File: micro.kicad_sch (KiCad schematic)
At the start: 19 parts, among them U101 STM32G474RETx

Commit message: Added SPI
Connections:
- net DIR1: now also U101.43 (PA9); no longer U101.21 (PA7)
- net DIR2: now also U101.45 (PA11); no longer U101.43 (PA9)
- net SPI_SCK: now reaches U101.19 (PA5)
- net SPI_MISO: now reaches U101.20 (PA6)
- new net SPI_MOSI: U101.21 (PA7)
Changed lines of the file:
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@@
+	(wire
+		(pts
+			(xy 156.21 54.61) (xy 170.18 54.61)
+		)
+		(stroke
+			(width 0)
+			(type default)
+		)
+	)
 	(wire
 		(pts
@@
 	(wire
 		(pts
+			(xy 156.21 64.77) (xy 201.93 64.77)
+		)
+		(stroke
+			(width 0)
+			(type default)
+		)
+	)
+	(wire
+		(pts
 			(xy 82.55 46.99) (xy 120.65 46.99)
 		)
@@
 	(wire
 		(pts
-			(xy 156.21 59.69) (xy 201.93 59.69)
-		)
-		(stroke
-			(width 0)
-			(type default)
-		)
-	)
-	(wire
-		(pts
 			(xy 156.21 80.01) (xy 170.18 80.01)
 		)
@@
 	(wire
 		(pts
+			(xy 156.21 59.69) (xy 170.18 59.69)
+		)
+		(stroke
+			(width 0)
+			(type default)
+		)
+	)
+	(wire
+		(pts
 			(xy 143.51 30.48) (xy 140.97 30.48)
 		)
@@
 	(wire
 		(pts
-			(xy 156.21 64.77) (xy 201.93 64.77)
-		)
-		(stroke
-			(width 0)
-			(type default)
-		)
-	)
-	(wire
-		(pts
 			(xy 184.15 49.53) (xy 190.5 49.53)
 		)
@@
 	(wire
 		(pts
+			(xy 156.21 69.85) (xy 201.93 69.85)
+		)
+		(stroke
+			(width 0)
+			(type default)
+		)
+	)
+	(wire
+		(pts
 			(xy 240.03 151.13) (xy 240.03 147.32)
 		)
@@
 		(pts
 			(xy 240.03 147.32) (xy 240.03 143.51)
+		)
+		(stroke
+			(width 0)
+			(type default)
+		)
+	)
+	(wire
+		(pts
+			(xy 156.21 57.15) (xy 170.18 57.15)
 		)
 		(stroke
@@
 		)
 	)
+	(hierarchical_label "SPI_MOSI"
+		(shape input)
+		(at 170.18 59.69 0)
+		(effects
+			(font
+				(size 1.27 1.27)
+			)
+			(justify left)
+		)
+	)
 	(hierarchical_label "T_SWO"
 		(shape bidirectional)
@@
 	(hierarchical_label "DIR2"
 		(shape output)
-		(at 201.93 64.77 0)
+		(at 201.93 69.85 0)
 		(effects
 			(font
@@
 		)
 	)
+	(hierarchical_label "SPI_SCK"
+		(shape input)
+		(at 170.18 54.61 0)
+		(effects
+			(font
+				(size 1.27 1.27)
+			)
+			(justify left)
+		)
+	)
 	(hierarchical_label "DIR1"
 		(shape output)
-		(at 201.93 59.69 0)
+		(at 201.93 64.77 0)
 		(effects
 			(font
@@
 		)
 	)
+	(hierarchical_label "SPI_MISO"
+		(shape output)
+		(at 170.18 57.15 0)
+		(effects
+			(font
+				(size 1.27 1.27)
+			)
+			(justify left)
+		)
+	)

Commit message: starting layout
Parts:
- R501: renamed from R214; footprint Resistor_SMD:R_0805_2012Metric_Pad1.20x1.40mm_HandSolder -> Resistor_SMD:R_0603_1608Metric_Pad0.98x0.95mm_HandSolder
- R502: renamed from R206; footprint Resistor_SMD:R_0805_2012Metric_Pad1.20x1.40mm_HandSolder -> Resistor_SMD:R_0603_1608Metric_Pad0.98x0.95mm_HandSolder
- R503: renamed from R207; footprint Resistor_SMD:R_0805_2012Metric_Pad1.20x1.40mm_HandSolder -> Resistor_SMD:R_0603_1608Metric_Pad0.98x0.95mm_HandSolder
- R504: renamed from R226; footprint Resistor_SMD:R_0805_2012Metric_Pad1.20x1.40mm_HandSolder -> Resistor_SMD:R_0603_1608Metric_Pad0.98x0.95mm_HandSolder
- R505: renamed from R210; footprint Resistor_SMD:R_0805_2012Metric_Pad1.20x1.40mm_HandSolder -> Resistor_SMD:R_0603_1608Metric_Pad0.98x0.95mm_HandSolder
- R506: renamed from R211; footprint Resistor_SMD:R_0805_2012Metric_Pad1.20x1.40mm_HandSolder -> Resistor_SMD:R_0603_1608Metric_Pad0.98x0.95mm_HandSolder
- R507: renamed from R208; footprint Resistor_SMD:R_0805_2012Metric_Pad1.20x1.40mm_HandSolder -> Resistor_SMD:R_0603_1608Metric_Pad0.98x0.95mm_HandSolder
- R508: renamed from R209; footprint Resistor_SMD:R_0805_2012Metric_Pad1.20x1.40mm_HandSolder -> Resistor_SMD:R_0603_1608Metric_Pad0.98x0.95mm_HandSolder
- renumbered C207 to C501, C208 to C502, C218 to C503, C206 to C504, C205 to C505, C204 to C506, C203 to C507, R227 to R509, R228 to R510, R232 to R511, U101 to U501
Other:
- moved on the sheet: R509, R510

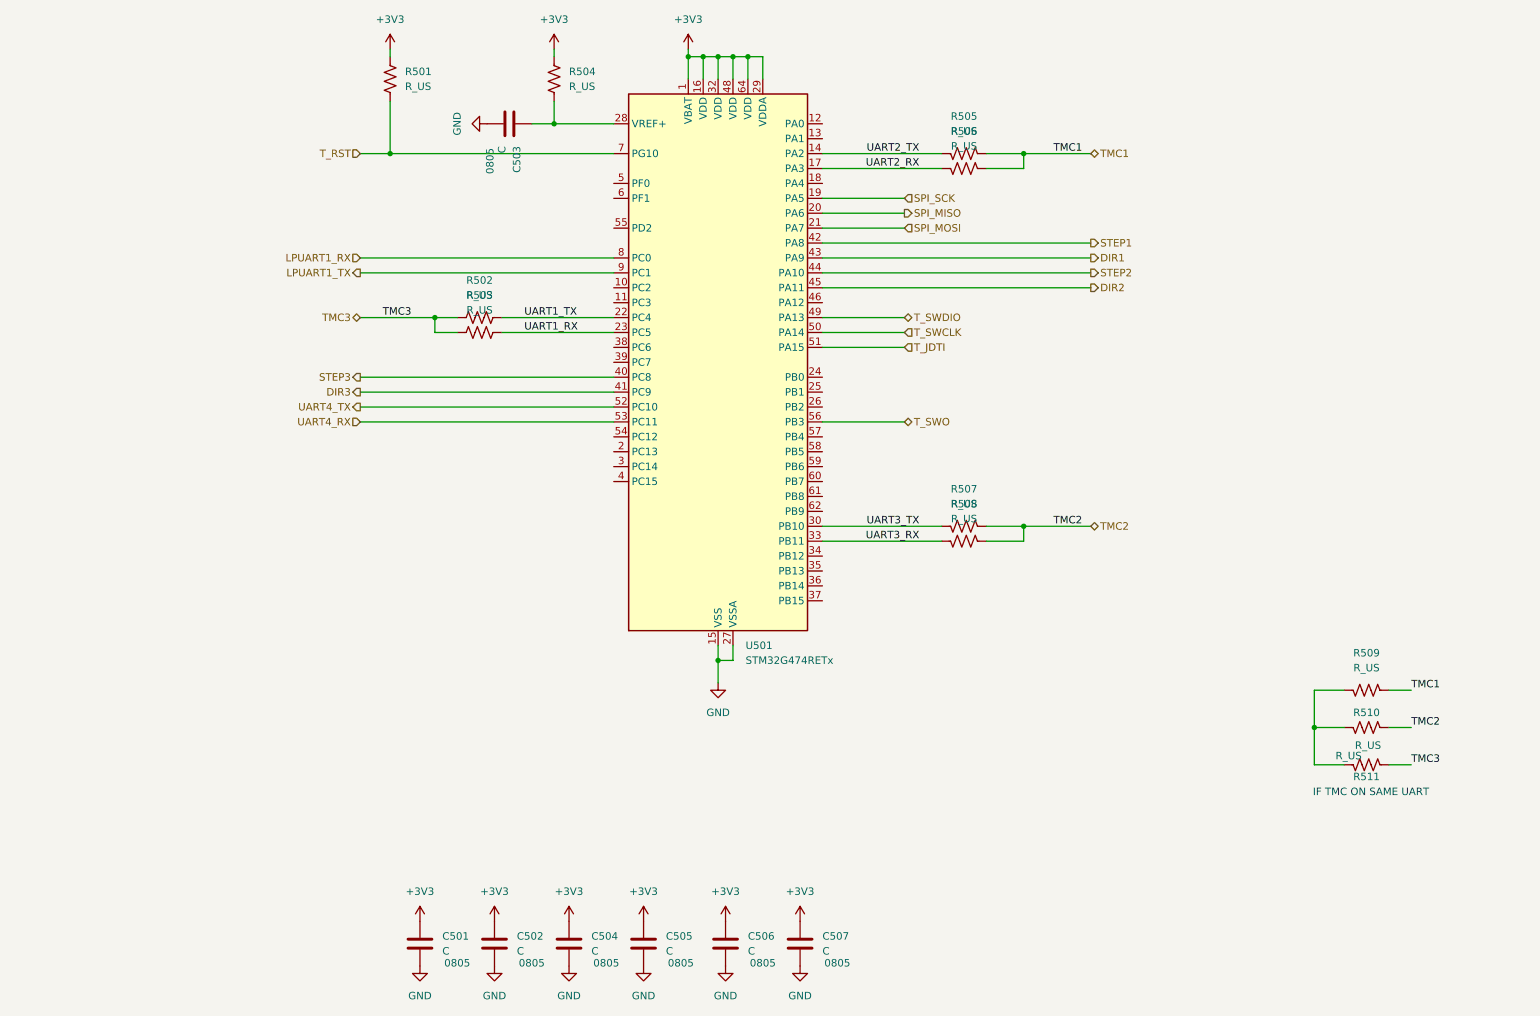
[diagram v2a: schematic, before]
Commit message: Add net class
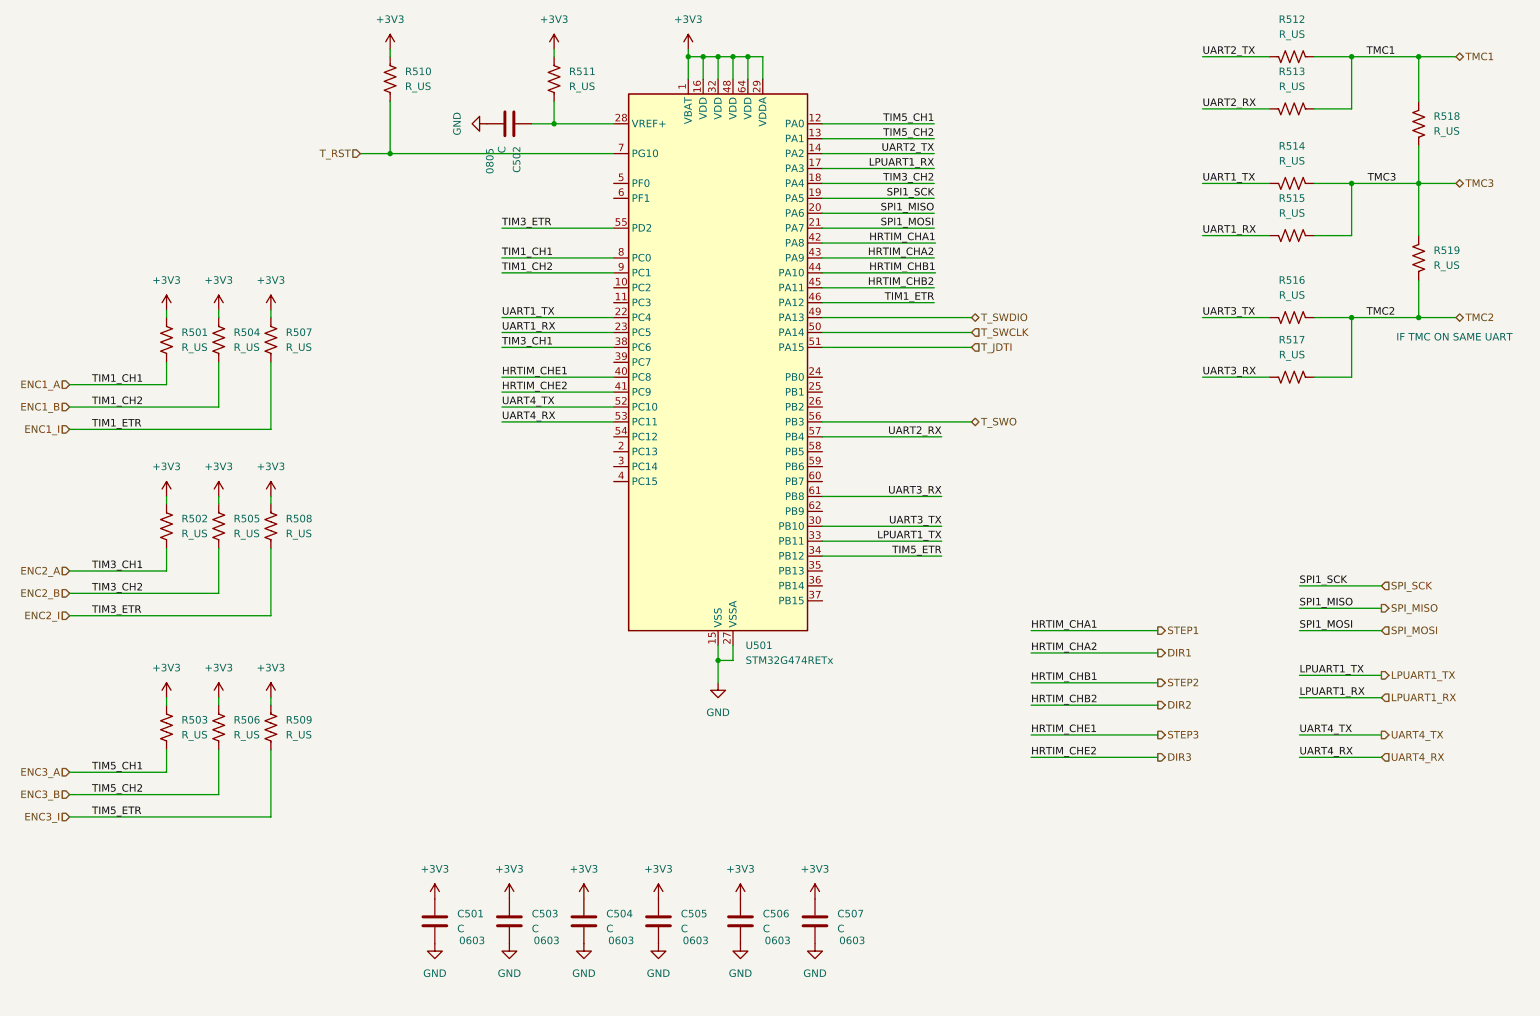
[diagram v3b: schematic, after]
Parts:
- removed C502: C, Capacitor_SMD:C_0805_2012Metric_Pad1.18x1.45mm_HandSolder, symbol Device:C
- removed R510, R511: R_US, Resistor_SMD:R_0805_2012Metric_Pad1.20x1.40mm_HandSolder, symbol Device:R_US
- added C503: C, Capacitor_SMD:C_0603_1608Metric_Pad1.08x0.95mm_HandSolder, symbol Device:C
- added R501, R502, R503, R504, R505, R506, R507, R508: R_US, Resistor_SMD:R_0603_1608Metric_Pad0.98x0.95mm_HandSolder, symbol Device:R_US
- added R518, R519: R_US, Resistor_SMD:R_0805_2012Metric_Pad1.20x1.40mm_HandSolder, symbol Device:R_US
- C501, C504, C505, C506, C507: footprint Capacitor_SMD:C_0805_2012Metric_Pad1.18x1.45mm_HandSolder -> Capacitor_SMD:C_0603_1608Metric_Pad1.08x0.95mm_HandSolder; Size 0805 -> 0603
- R509: footprint Resistor_SMD:R_0805_2012Metric_Pad1.20x1.40mm_HandSolder -> Resistor_SMD:R_0603_1608Metric_Pad0.98x0.95mm_HandSolder
- renumbered C503 to C502, R501 to R510, R504 to R511, R505 to R512, R506 to R513, R502 to R514, R503 to R515, R507 to R516, R508 to R517
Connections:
- net +3V3: now also R509.2, C503.1, R501.2, R502.2, R503.2, R504.2, R505.2, R506.2, R507.2, R508.2
- net GND: now also C503.2
- net LPUART1_RX: now also U501.17 (PA3); no longer U501.8 (PC0)
- net LPUART1_TX: now also U501.33 (PB11); no longer U501.9 (PC1)
- net TMC1: now also R518.1; no longer R509.1
- net TMC2: now also R519.2
- net TMC3: now also R518.2, R519.1
- net UART2_RX: now also U501.57 (PB4); no longer U501.17 (PA3)
- net UART3_RX: now also U501.61 (PB8); no longer U501.33 (PB11)
- net ENC3_A: now reaches U501.12 (PA0)
- net ENC3_A: now also R503.1
- net ENC3_B: now reaches U501.13 (PA1)
- net ENC3_B: now also R506.1
- net ENC2_B: now reaches U501.18 (PA4)
- net ENC2_B: now also R505.1
- net ENC3_I: now reaches U501.34 (PB12)
- net ENC3_I: now also R509.1
- net ENC2_A: now reaches U501.38 (PC6)
- net ENC2_A: now also R502.1
- net ENC1_I: now reaches U501.46 (PA12)
- net ENC1_I: now also R507.1
- net ENC2_I: now reaches U501.55 (PD2)
- net ENC2_I: now also R508.1
- new net ENC1_A: R501.1, U501.8 (PC0)
- new net ENC1_B: R504.1, U501.9 (PC1)
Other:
- moved on the sheet: C501, R512, R513, R514, R515, R516, R517

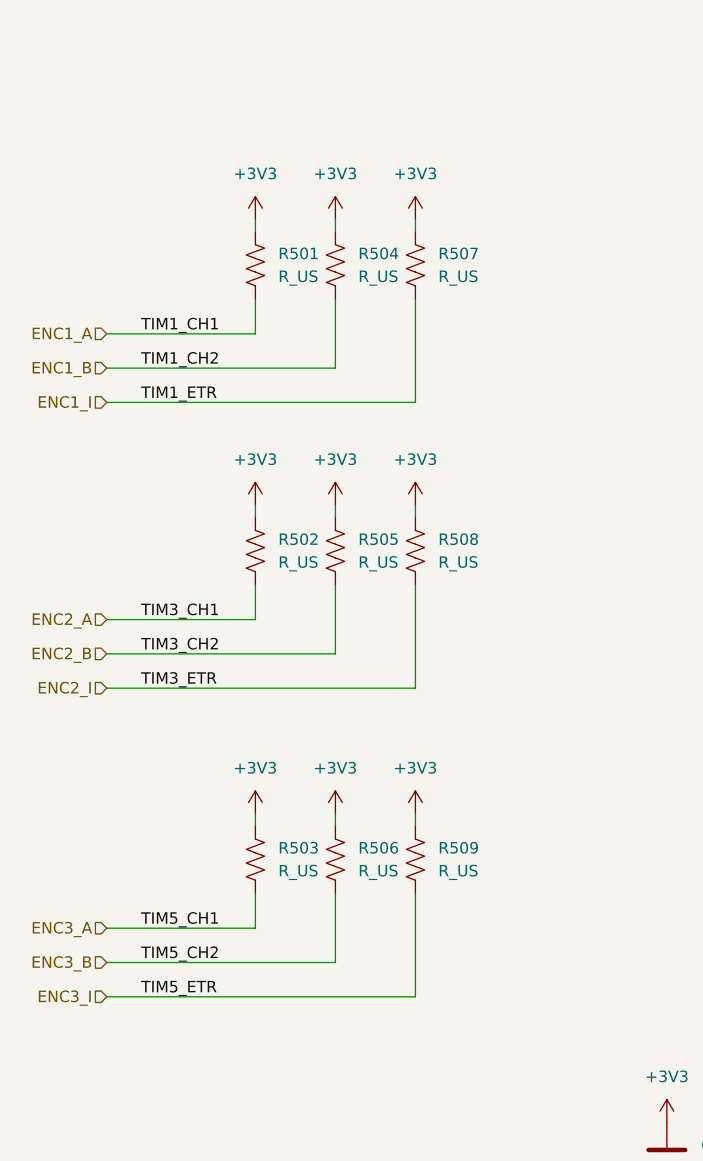
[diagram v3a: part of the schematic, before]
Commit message: move encoder pull up resistor to tmc sheet
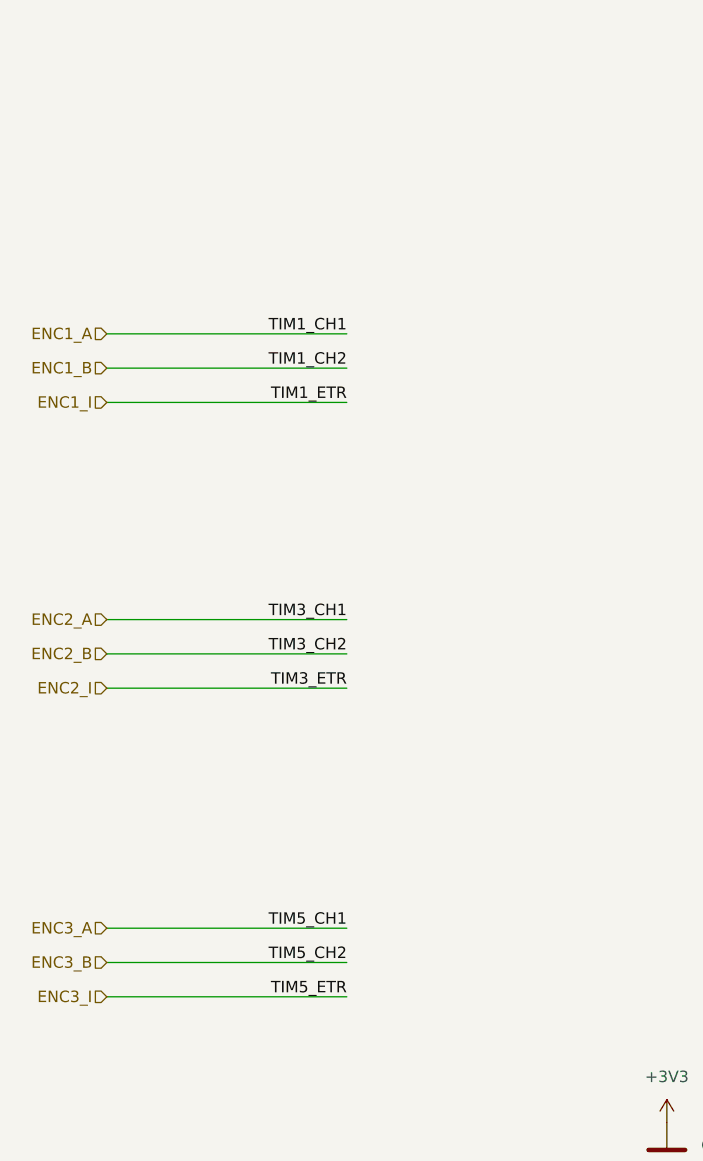
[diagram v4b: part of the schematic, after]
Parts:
- removed R501, R502, R503, R504, R505, R506, R507, R508, R509: R_US, Resistor_SMD:R_0603_1608Metric_Pad0.98x0.95mm_HandSolder, symbol Device:R_US

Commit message: AHHHAHAHAHHAH
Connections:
- net DIR2: now also U501.41 (PC9); no longer U501.45 (PA11)
- net DIR3: now also U501.45 (PA11); no longer U501.41 (PC9)
- net ENC2_A: now also U501.12 (PA0); no longer U501.38 (PC6)
- net ENC2_B: now also U501.13 (PA1); no longer U501.18 (PA4)
- net ENC2_I: now also U501.34 (PB12); no longer U501.55 (PD2)
- net ENC3_A: now also U501.38 (PC6); no longer U501.12 (PA0)
- net ENC3_B: now also U501.18 (PA4); no longer U501.13 (PA1)
- net ENC3_I: now also U501.55 (PD2); no longer U501.34 (PB12)
- net STEP2: now also U501.40 (PC8); no longer U501.44 (PA10)
- net STEP3: now also U501.44 (PA10); no longer U501.40 (PC8)
- net TMC2: now also R514.1, R515.1; no longer R516.1, R517.1
- net TMC3: now also R516.1, R517.1; no longer R514.1, R515.1
- net UART3_TX: now also U501.62 (PB9); no longer U501.30 (PB10)
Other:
- moved on the sheet: R514, R515, R516, R517

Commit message: before trying new µC orientation
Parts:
- removed C502: C, Capacitor_SMD:C_0805_2012Metric_Pad1.18x1.45mm_HandSolder, symbol Device:C
- added C508: C, Capacitor_SMD:C_0603_1608Metric_Pad1.08x0.95mm_HandSolder, symbol Device:C
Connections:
- net GND: now also C508.1
- net at R511.1, U501.28 (VREF+): now also C508.2
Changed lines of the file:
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@@
+	(symbol
+		(lib_id "Device:C")
+		(at 102.87 41.91 90)
+		(unit 1)
+		(exclude_from_sim no)
+		(in_bom yes)
+		(on_board yes)
+		(dnp no)
+		(property "Reference" "C508"
+			(at 101.5999 38.1 0)
+			(effects
+				(font
+					(size 1.27 1.27)
+				)
+				(justify left)
+			)
+		)
+		(property "Value" "C"
+			(at 104.1399 38.1 0)
+			(effects
+				(font
+					(size 1.27 1.27)
+				)
+				(justify left)
+			)
+		)
+		(property "Footprint" "Capacitor_SMD:C_0603_1608Metric_Pad1.08x0.95mm_HandSolder"
+			(at 106.68 40.9448 0)
+			(effects
+				(font
+					(size 1.27 1.27)
+				)
+				(hide yes)
+			)
+		)
+		(property "Datasheet" "~"
+			(at 102.87 41.91 0)
+			(effects
+				(font
+					(size 1.27 1.27)
+				)
+				(hide yes)
+			)
+		)
+		(property "Description" "Unpolarized capacitor"
+			(at 102.87 41.91 0)
+			(effects
+				(font
+					(size 1.27 1.27)
+				)
+				(hide yes)
+			)
+		)
+		(property "Size" "0603"
+			(at 106.172 35.56 0)
+			(effects
+				(font
+					(size 1.27 1.27)
+				)
+			)
+		)
+		(pin "1"
+		)
+		(pin "2"
+		)
+		(instances
+			(project "Carte_moteur"
+				(path "/5d858058-eb89-4613-a7ba-0652b9f0936c/28bdad79-5371-4e22-98e6-66bca5f68bc6"
+					(reference "C508")
+					(unit 1)
+				)
+			)
+		)
+	)
 	(symbol
 		(lib_id "Device:C")
@@
 					(unit 1)
 				)
-			)
-		)
-	)
-	(symbol
-		(lib_id "Device:C")
-		(at 102.87 41.91 270)
-		(unit 1)
-		(exclude_from_sim no)
-		(in_bom yes)
-		(on_board yes)
-		(dnp no)
-		(property "Reference" "C502"
-			(at 104.1401 45.72 0)
-			(effects
-				(font
-					(size 1.27 1.27)
-				)
-				(justify left)
-			)
-		)
-		(property "Value" "C"
-			(at 101.6001 45.72 0)
-			(effects
-				(font
-					(size 1.27 1.27)
-				)
-				(justify left)
-			)
-		)
-		(property "Footprint" "Capacitor_SMD:C_0805_2012Metric_Pad1.18x1.45mm_HandSolder"
-			(at 99.06 42.8752 0)
-			(effects
-				(font
-					(size 1.27 1.27)
-				)
-				(hide yes)
-			)
-		)
-		(property "Datasheet" "~"
-			(at 102.87 41.91 0)
-			(effects
-				(font
-					(size 1.27 1.27)
-				)
-				(hide yes)
-			)
-		)
-		(property "Description" "Unpolarized capacitor"
-			(at 102.87 41.91 0)
-			(effects
-				(font
-					(size 1.27 1.27)
-				)
-				(hide yes)
-			)
-		)
-		(property "Size" "0805"
-			(at 99.568 48.26 0)
-			(effects
-				(font
-					(size 1.27 1.27)
-				)
-			)
-		)
-		(pin "1"
-		)
-		(pin "2"
-		)
-		(instances
-			(project "Carte_moteur"
-				(path "/5d858058-eb89-4613-a7ba-0652b9f0936c/28bdad79-5371-4e22-98e6-66bca5f68bc6"
-					(reference "C502")
-					(unit 1)
-				)

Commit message: almost done
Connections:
- net DIR1: now also U501.41 (PC9); no longer U501.43 (PA9)
- net DIR2: now also U501.43 (PA9); no longer U501.41 (PC9)
- net ENC1_A: now also U501.12 (PA0); no longer U501.8 (PC0)
- net ENC1_B: now also U501.13 (PA1); no longer U501.9 (PC1)
- net ENC1_I: now also U501.34 (PB12); no longer U501.46 (PA12)
- net ENC2_A: now also U501.8 (PC0); no longer U501.12 (PA0)
- net ENC2_B: now also U501.9 (PC1); no longer U501.13 (PA1)
- net ENC2_I: now also U501.46 (PA12); no longer U501.34 (PB12)
- net STEP1: now also U501.40 (PC8); no longer U501.42 (PA8)
- net STEP2: now also U501.42 (PA8); no longer U501.40 (PC8)
- net TMC1: now also R514.1, R515.1; no longer R512.1, R513.1
- net TMC2: now also R512.1, R513.1; no longer R514.1, R515.1
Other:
- moved on the sheet: R512, R513, R514, R515

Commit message: tracks done
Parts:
- removed C501, C507: C, Capacitor_SMD:C_0603_1608Metric_Pad1.08x0.95mm_HandSolder, symbol Device:C
